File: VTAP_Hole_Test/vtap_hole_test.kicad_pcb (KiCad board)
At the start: 2 copper layers, 38 x 21 mm, 8 parts

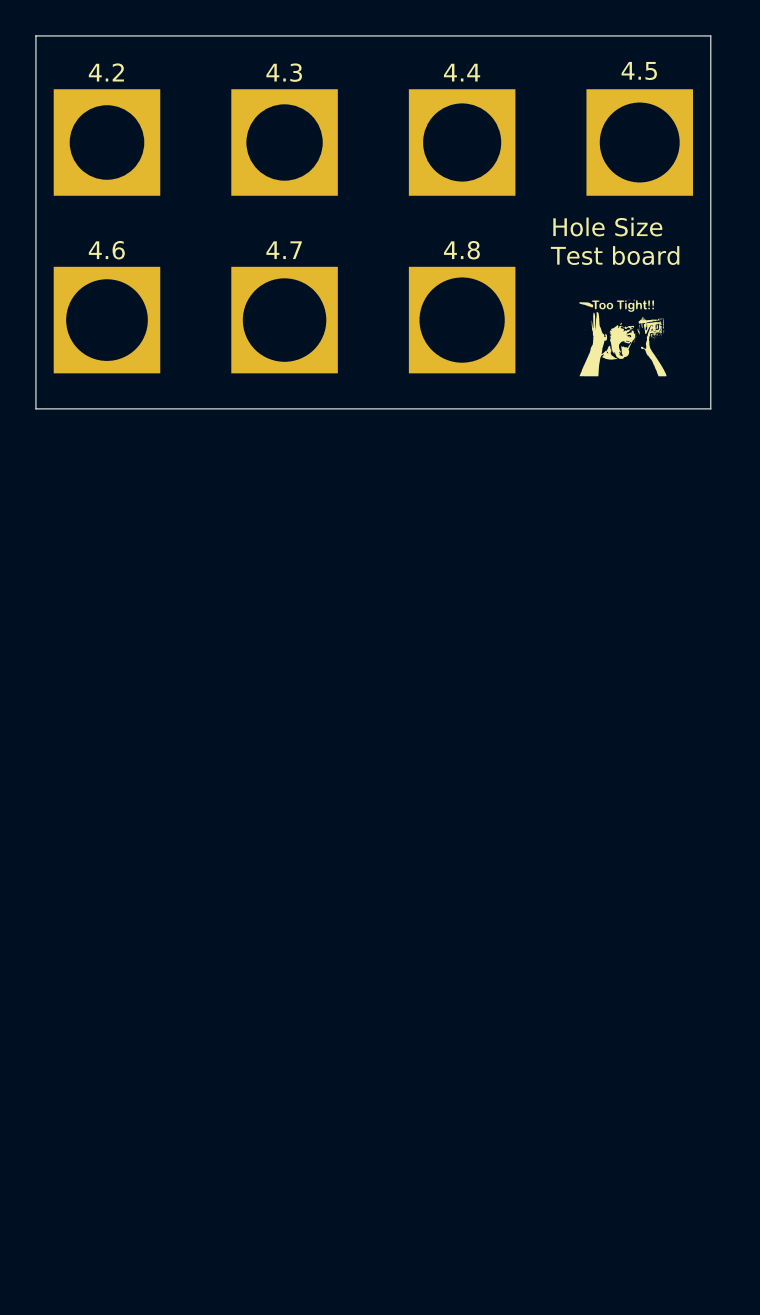
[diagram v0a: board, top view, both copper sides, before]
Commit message: vtap hole test board
pads of size 4.20-4.80 with 0.02 increment
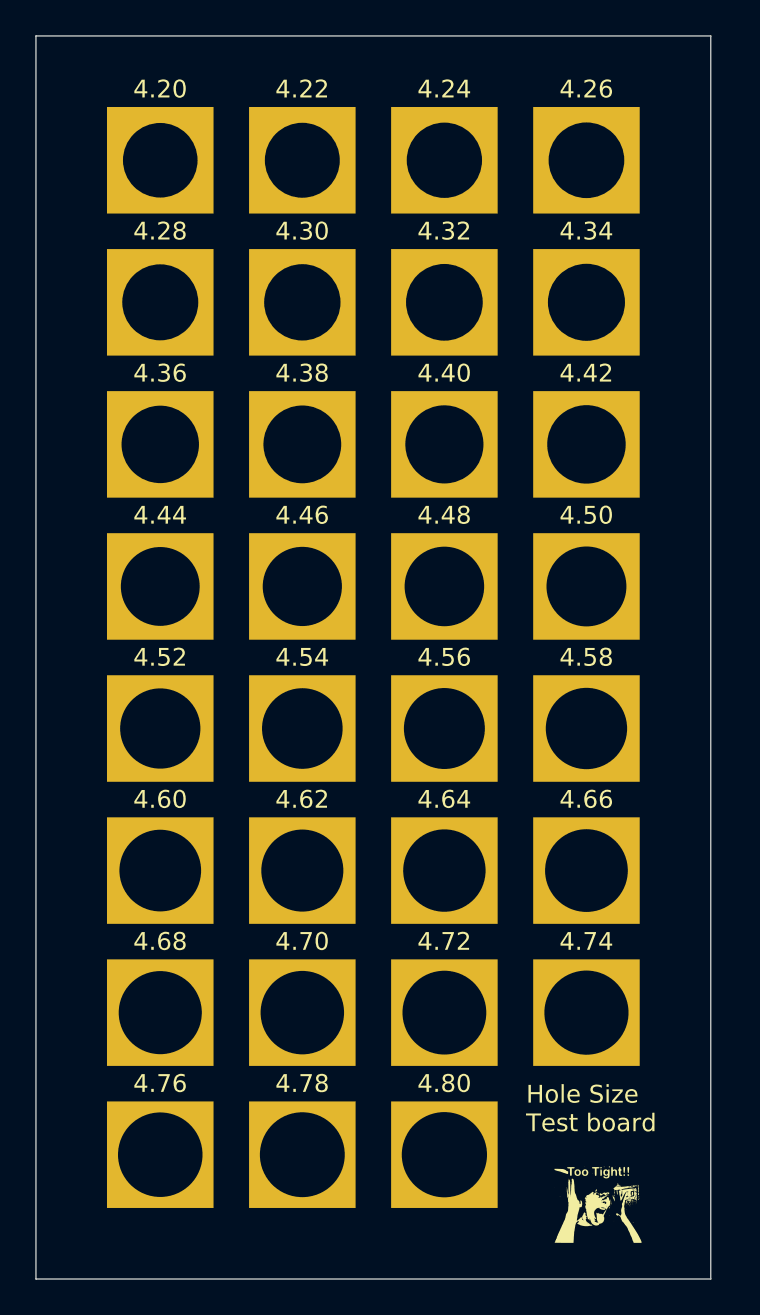
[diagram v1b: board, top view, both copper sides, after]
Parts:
- removed 4.2, 4.3, 4.4, 4.5, 4.6, 4.7, 4.8: TestPoint_Pad_D4.0mm, TestPoint:TestPoint_Pad_D4.0mm
- added REF**: Untitled, dumshit:Untitled, F.Cu at (33.0, 31.0)
- moved G*** 48.8 mm to (57.6, 89.8)
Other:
- board size 38 x 21 mm -> 38 x 70 mm
